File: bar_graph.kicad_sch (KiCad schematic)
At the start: 9 parts, among them U4 74LS163, U5 74LS163, U6 74LS163, U7 74LS163, U8 74LS163

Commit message: V1.1-last Kicad v7 version
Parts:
- D4, D5: footprint footprints:LED_Bar_Graph_10_SEG -> Homebrew-CPU-PCB:LED_Bar_Graph_10_SEG; symbol homebrew_cpu:LED_BAR_GRAPH_10_SEG -> Homebrew-CPU-PCB:LED_BAR_GRAPH_10_SEG
- RN1, RN2: footprint footprints:R_Array_SIP11 -> Homebrew-CPU-PCB:R_Array_SIP11; symbol homebrew_cpu:R_Network10 -> Homebrew-CPU-PCB:R_Network10
- U4, U5, U6, U7, U8: footprint footprints:DIP-16_W7.62mm_Socket -> Homebrew-CPU-PCB:DIP-16_W7.62mm_Socket; symbol homebrew_cpu:74LS163 -> Homebrew-CPU-PCB:74LS163
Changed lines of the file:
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@@
     )
   )
-  (symbol (lib_id "homebrew_cpu:R_Network10") (at 122.555 120.65 180) (unit 1)
+  (symbol (lib_name "R_Network10_1") (lib_id "Homebrew-CPU-PCB:R_Network10") (at 122.555 120.65 180) (unit 1)
     (in_bom yes) (on_board yes) (dnp no)
     (property "Reference" "RN1" (at 137.795 118.745 90)
@@
       (effects (font (size 1 1)) (justify left))
     )
-    (property "Footprint" "footprints:R_Array_SIP11" (at 107.95 120.65 90)
+    (property "Footprint" "Homebrew-CPU-PCB:R_Array_SIP11" (at 107.95 120.65 90)
       (effects (font (size 1 1)) hide)
     )
@@
     )
   )
-  (symbol (lib_id "homebrew_cpu:74LS163") (at 223.52 144.78 90) (unit 1)
+  (symbol (lib_id "Homebrew-CPU-PCB:74LS163") (at 223.52 144.78 90) (unit 1)
     (in_bom yes) (on_board yes) (dnp no)
     (property "Reference" "U4" (at 207.645 135.89 90)
@@
       (effects (font (size 1 1)) (justify left))
     )
-    (property "Footprint" "footprints:DIP-16_W7.62mm_Socket" (at 223.52 144.78 0)
+    (property "Footprint" "Homebrew-CPU-PCB:DIP-16_W7.62mm_Socket" (at 223.52 144.78 0)
       (effects (font (size 1 1)) hide)
     )
@@
     )
   )
-  (symbol (lib_id "homebrew_cpu:74LS163") (at 57.15 144.145 90) (unit 1)
+  (symbol (lib_name "74LS163_4") (lib_id "Homebrew-CPU-PCB:74LS163") (at 57.15 144.145 90) (unit 1)
     (in_bom yes) (on_board yes) (dnp no)
     (property "Reference" "U8" (at 41.91 135.255 90)
@@
       (effects (font (size 1 1)) (justify left))
     )
-    (property "Footprint" "footprints:DIP-16_W7.62mm_Socket" (at 57.15 144.145 0)
+    (property "Footprint" "Homebrew-CPU-PCB:DIP-16_W7.62mm_Socket" (at 57.15 144.145 0)
       (effects (font (size 1 1)) hide)
     )
@@
     )
   )
-  (symbol (lib_id "homebrew_cpu:74LS163") (at 223.52 48.26 270) (unit 1)
+  (symbol (lib_name "74LS163_3") (lib_id "Homebrew-CPU-PCB:74LS163") (at 223.52 48.26 270) (unit 1)
     (in_bom yes) (on_board yes) (dnp no)
     (property "Reference" "U5" (at 206.375 39.37 90)
@@
       (effects (font (size 1 1)) (justify left))
     )
-    (property "Footprint" "footprints:DIP-16_W7.62mm_Socket" (at 223.52 48.26 0)
+    (property "Footprint" "Homebrew-CPU-PCB:DIP-16_W7.62mm_Socket" (at 223.52 48.26 0)
       (effects (font (size 1 1)) hide)
     )
@@
     )
   )
-  (symbol (lib_id "homebrew_cpu:R_Network10") (at 157.48 120.65 180) (unit 1)
+  (symbol (lib_id "Homebrew-CPU-PCB:R_Network10") (at 157.48 120.65 180) (unit 1)
     (in_bom yes) (on_board yes) (dnp no)
     (property "Reference" "RN2" (at 172.72 119.38 90)
@@
       (effects (font (size 1 1)) (justify left))
     )
-    (property "Footprint" "footprints:R_Array_SIP11" (at 142.875 120.65 90)
+    (property "Footprint" "Homebrew-CPU-PCB:R_Array_SIP11" (at 142.875 120.65 90)
       (effects (font (size 1 1)) hide)
     )
@@
     )
   )
-  (symbol (lib_id "homebrew_cpu:74LS163") (at 55.245 48.26 270) (unit 1)
+  (symbol (lib_name "74LS163_1") (lib_id "Homebrew-CPU-PCB:74LS163") (at 55.245 48.26 270) (unit 1)
     (in_bom yes) (on_board yes) (dnp no)
     (property "Reference" "U7" (at 40.64 39.37 90)
@@
       (effects (font (size 1 1)))
     )
-    (property "Footprint" "footprints:DIP-16_W7.62mm_Socket" (at 55.245 48.26 0)
+    (property "Footprint" "Homebrew-CPU-PCB:DIP-16_W7.62mm_Socket" (at 55.245 48.26 0)
       (effects (font (size 1 1)) hide)
     )
@@
     )
   )
-  (symbol (lib_id "homebrew_cpu:LED_BAR_GRAPH_10_SEG") (at 170.18 105.41 270) (unit 1)
+  (symbol (lib_id "Homebrew-CPU-PCB:LED_BAR_GRAPH_10_SEG") (at 170.18 105.41 270) (unit 1)
     (in_bom yes) (on_board yes) (dnp no)
     (property "Reference" "D5" (at 173.99 105.41 0)
@@
       (effects (font (size 1 1)) (justify left))
     )
-    (property "Footprint" "footprints:LED_Bar_Graph_10_SEG" (at 175.26 110.49 0)
+    (property "Footprint" "Homebrew-CPU-PCB:LED_Bar_Graph_10_SEG" (at 175.26 110.49 0)
       (effects (font (size 1 1)) (justify left) hide)
     )
@@
     )
   )
-  (symbol (lib_id "homebrew_cpu:LED_BAR_GRAPH_10_SEG") (at 135.255 105.41 270) (unit 1)
+  (symbol (lib_name "LED_BAR_GRAPH_10_SEG_1") (lib_id "Homebrew-CPU-PCB:LED_BAR_GRAPH_10_SEG") (at 135.255 105.41 270) (unit 1)
     (in_bom yes) (on_board yes) (dnp no)
     (property "Reference" "D4" (at 139.065 104.775 0)
@@
       (effects (font (size 1 1)) (justify left))
     )
-    (property "Footprint" "footprints:LED_Bar_Graph_10_SEG" (at 140.335 110.49 0)
+    (property "Footprint" "Homebrew-CPU-PCB:LED_Bar_Graph_10_SEG" (at 140.335 110.49 0)
       (effects (font (size 1 1)) (justify left) hide)
     )
@@
     )
   )
-  (symbol (lib_id "homebrew_cpu:74LS163") (at 130.175 48.26 270) (unit 1)
+  (symbol (lib_name "74LS163_2") (lib_id "Homebrew-CPU-PCB:74LS163") (at 130.175 48.26 270) (unit 1)
     (in_bom yes) (on_board yes) (dnp no)
     (property "Reference" "U6" (at 113.03 39.37 90)
@@
       (effects (font (size 1 1)) (justify left))
     )
-    (property "Footprint" "footprints:DIP-16_W7.62mm_Socket" (at 130.175 48.26 0)
-      (effects (font (size 1 1)) hide)
-    )
+    (property "Footprint" "Homebrew-CPU-PCB:DIP-16_W7.62mm_Socket" (at 130.175 48.26 0)
+      (effects (font (size 1 1)) hide)
+    )

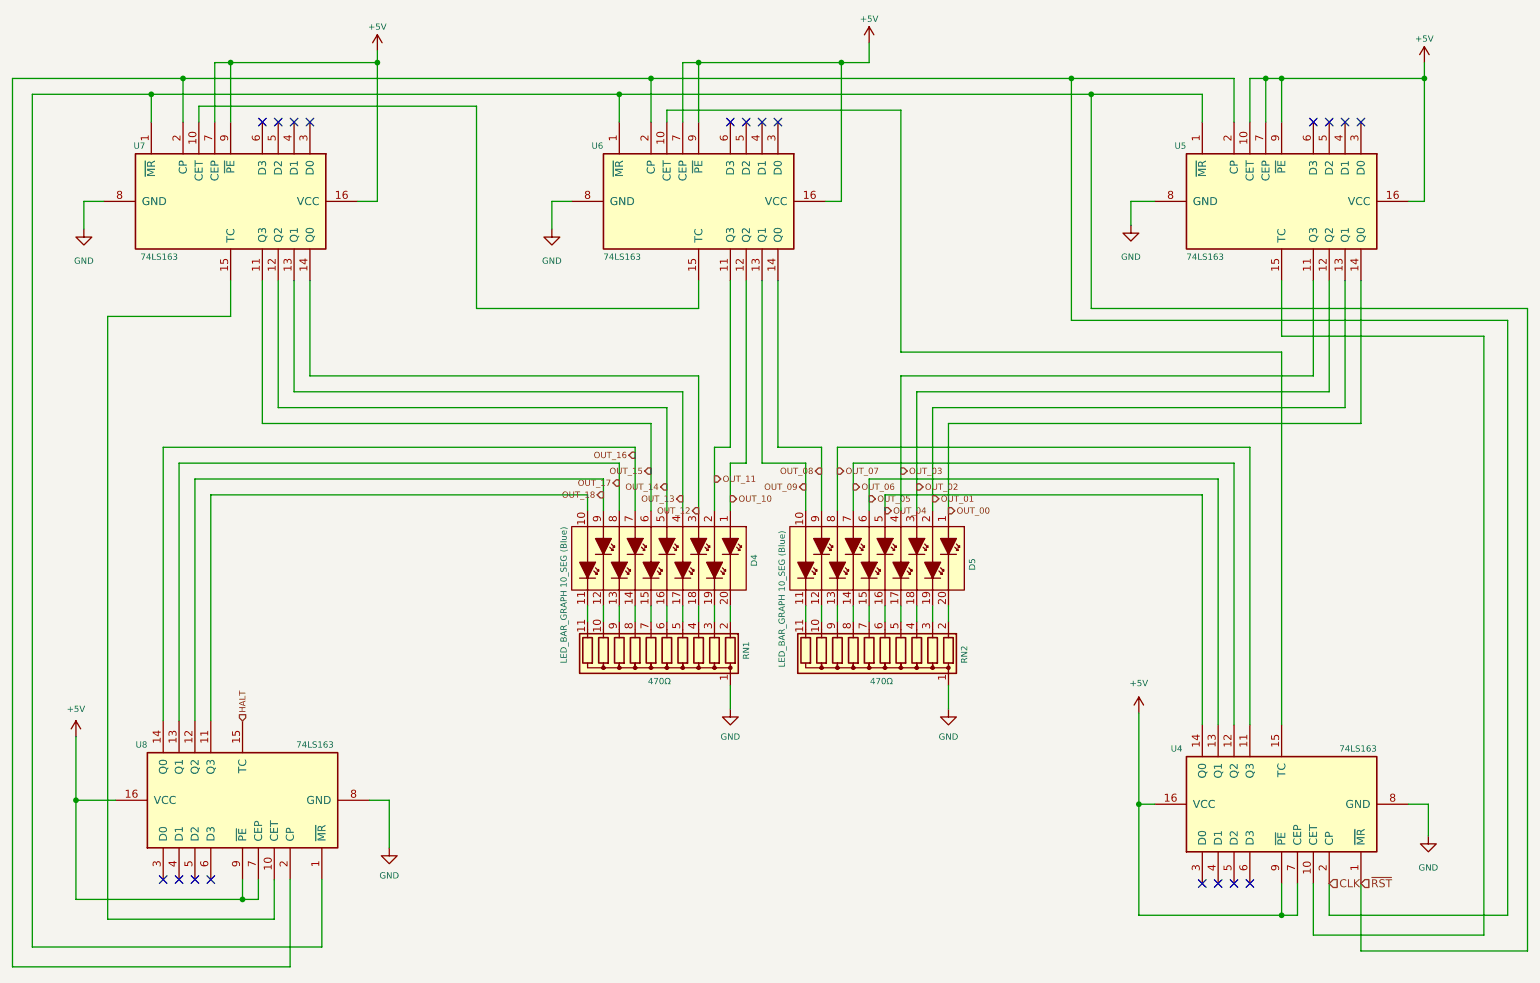
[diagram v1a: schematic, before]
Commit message: First KiCad v8 version.All ERC/DRC errors/warnings fixed - had to fix nets on left end of audio potentiometer so that they match. Weird.
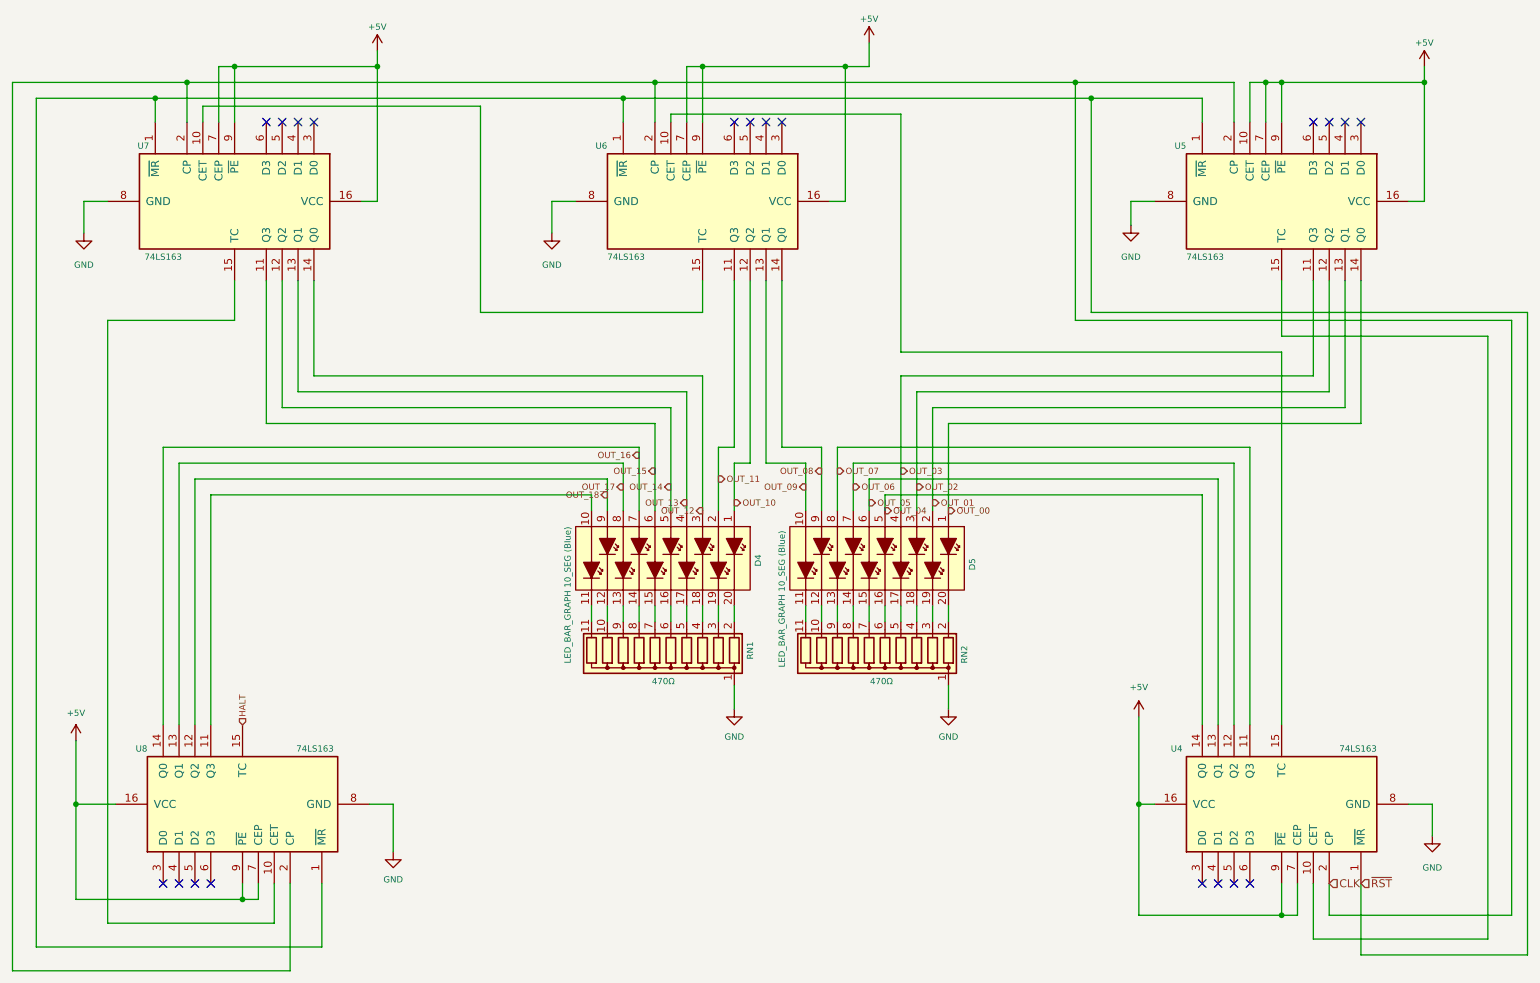
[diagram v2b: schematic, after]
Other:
- moved on the sheet: D4, RN1, U6, U7, U8
